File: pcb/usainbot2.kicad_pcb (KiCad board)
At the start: 2 copper layers, 157 x 131.5 mm, 21 parts, among them J1 BT_MOD, J2 QTR1-L, J3 QTR1-R, J4 QTR-6A, J5 M1, J6 BATT, J7 M2, SW1 SW_SPDT, SW2 SW_Push, U1 TB6612FNG_breakout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

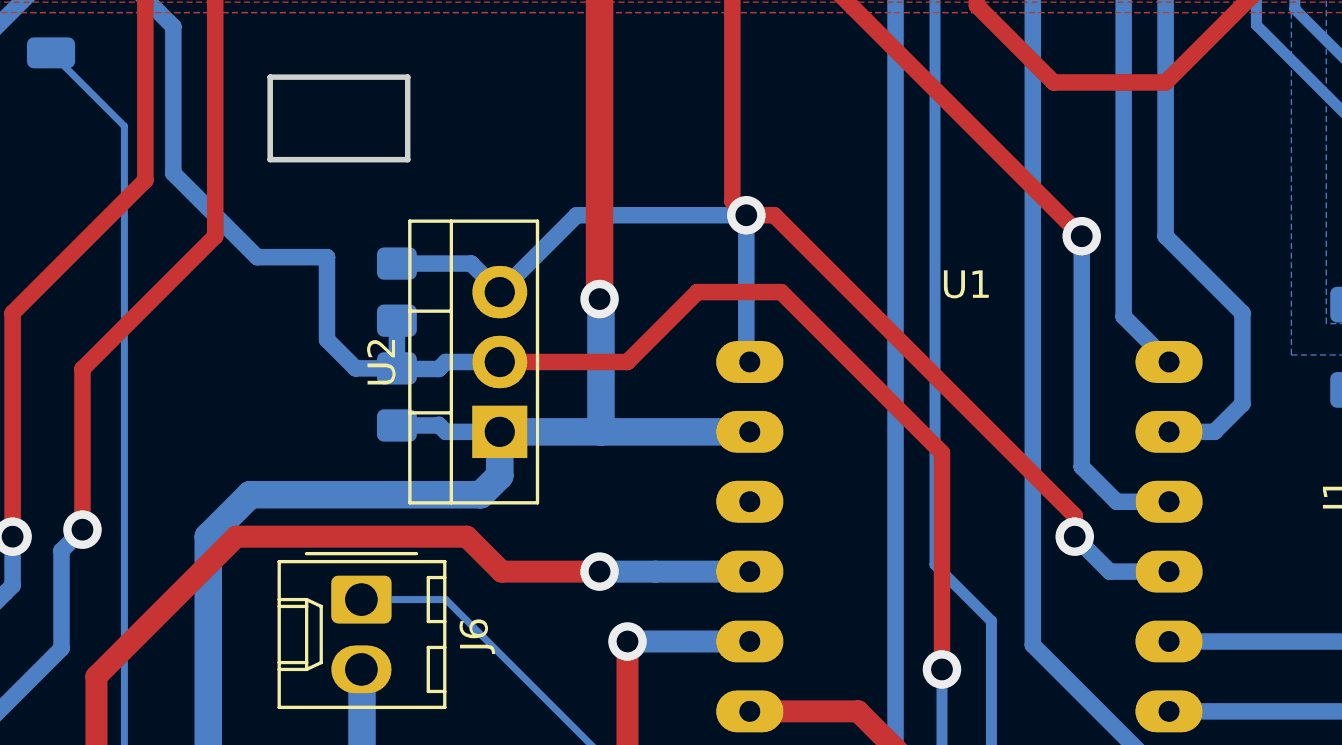
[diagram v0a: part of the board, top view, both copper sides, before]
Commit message: corrige error de diseño
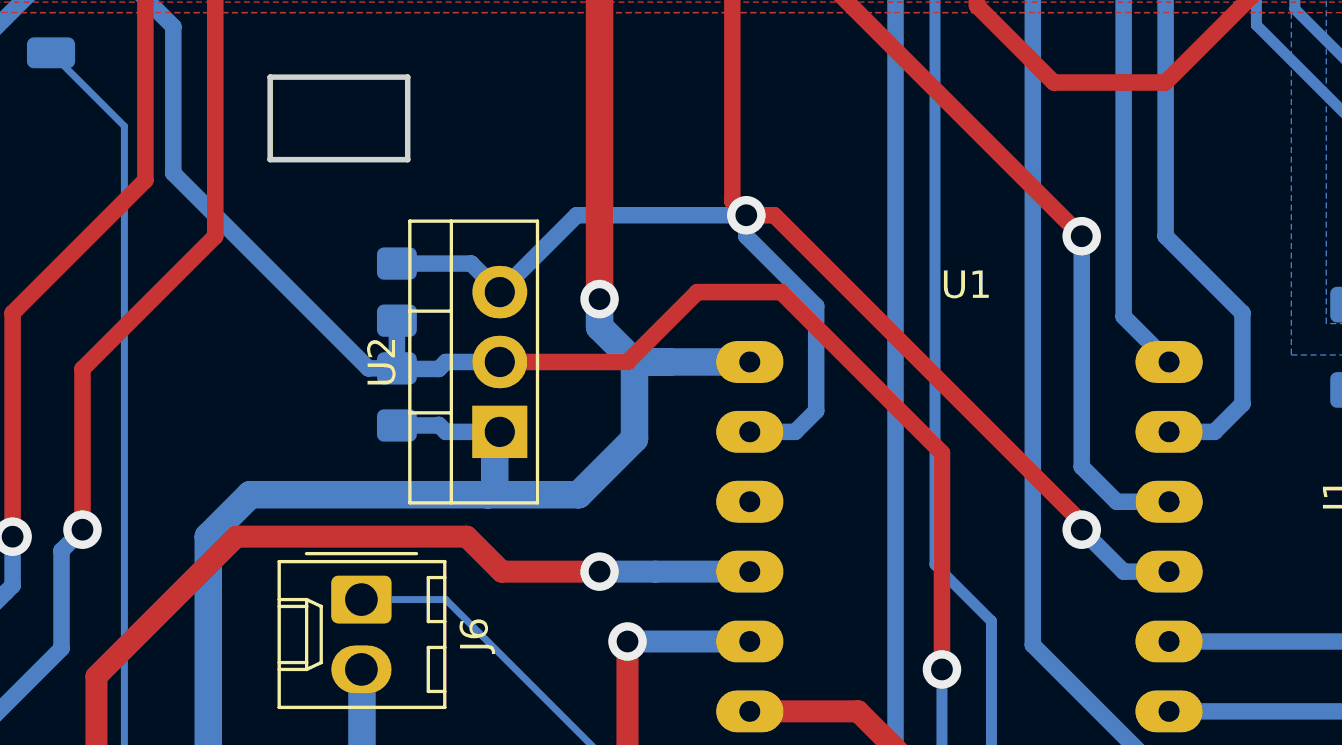
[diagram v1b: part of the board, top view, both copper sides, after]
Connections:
- U1 pad 1: +5V -> VCC
- U1 pad 2: VCC -> +5V
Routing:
- net +5V: track 279.5 -> 284.7 mm
- net VCC: track 82.6 -> 86.1 mm
- net GND: track 382.4 -> 380.6 mm
